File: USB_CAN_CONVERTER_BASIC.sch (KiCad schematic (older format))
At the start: 22 parts, among them P1 CONN_01X05, P2 CONN_01X02, P3 USB_A, P4 CONN_01X04, U1 STM32F042C6Ux, U2 PSD2CAN, U3 SN65HVD232D, U4 MCP1700T-3302E/TT, U5 USBLC6-2

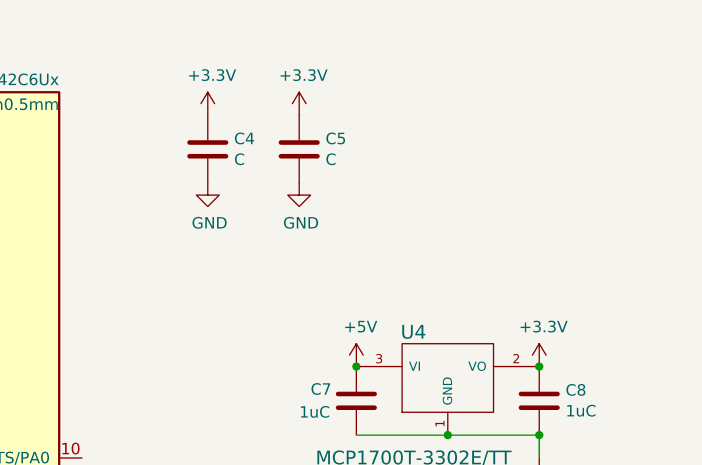
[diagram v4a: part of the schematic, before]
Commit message: Outline size reduction
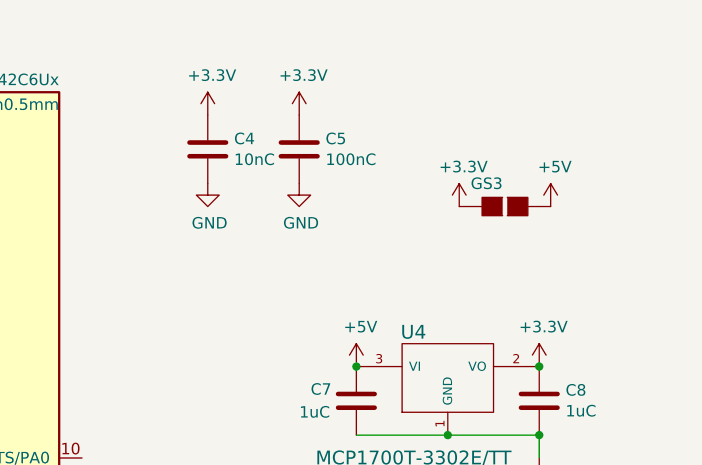
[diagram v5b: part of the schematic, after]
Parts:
- added GS3: GS2, Connect:GS2, symbol GS2
- C4: value C -> 10nC
- C5: value C -> 100nC
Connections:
- net +3V3: now also GS3.2 (G2)
- net +5V: now also GS3.1 (G1)
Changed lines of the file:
@@
 P 9100 1700
 F 0 "C4" H 9215 1746 50  0000 L CNN
-F 1 "C" H 9215 1655 50  0000 L CNN
+F 1 "10nC" H 9215 1655 50  0000 L CNN
 F 2 "Resistors_SMD:R_0805" H 9138 1550 50  0001 C CNN
 F 3 "" H 9100 1700 50  0000 C CNN
@@
 P 9500 1700
 F 0 "C5" H 9615 1746 50  0000 L CNN
-F 1 "C" H 9615 1655 50  0000 L CNN
+F 1 "100nC" H 9615 1655 50  0000 L CNN
 F 2 "Resistors_SMD:R_0805_HandSoldering" H 9538 1550 50  0001 C CNN
 F 3 "" H 9500 1700 50  0000 C CNN
@@
 	0    -1   -1   0
 $EndComp
+$Comp
+L GND #PWR15
+U 1 1 571ACD79
+P 9250 3350
+F 0 "#PWR15" H 9250 3100 50  0001 C CNN
+F 1 "GND" H 9350 3200 50  0000 C CNN
+F 2 "" H 9250 3350 50  0000 C CNN
+F 3 "" H 9250 3350 50  0000 C CNN
+	1    9250 3350
+	-1   0    0    1
+$EndComp
+$Comp
+L CONN_01X04 P4
+U 1 1 571E76C6
+P 9600 3500
+F 0 "P4" H 9677 3492 50  0000 L CNN
+F 1 "CONN_01X04" H 9678 3447 50  0001 L CNN
+F 2 "usb_ccb_custom:Pin_Header_Angled_1x04m" H 9677 3447 50  0001 L CNN
+F 3 "" H 9600 3500 50  0000 C CNN
+	1    9600 3500
+	1    0    0    -1
+$EndComp
+$Comp
+L +5V #PWR16
+U 1 1 571E7816
+P 9400 3350
+F 0 "#PWR16" H 9400 3200 50  0001 C CNN
+F 1 "+5V" H 9418 3523 50  0000 C CNN
+F 2 "" H 9400 3350 50  0000 C CNN
+F 3 "" H 9400 3350 50  0000 C CNN
+	1    9400 3350
+	1    0    0    -1
+$EndComp
+Text Label 8850 3550 0    60   ~ 0
+USART1_TX
+Text Label 8850 3650 0    60   ~ 0
+USART1_RX
+$Comp
+L CONN_01X05 P1
+U 1 1 57800591
+P 950 2050
+F 0 "P1" H 869 1711 50  0000 C CNN
+F 1 "CONN_01X05" H 869 1710 50  0001 C CNN
+F 2 "usb_ccb_custom:swd_smd_conn5" H 869 1711 50  0001 C CNN
+F 3 "" H 950 2050 50  0000 C CNN
+	1    950  2050
+	-1   0    0    1
+$EndComp
+$Comp
+L +3.3V #PWR1
+U 1 1 57800AA2
+P 1150 2250
+F 0 "#PWR1" H 1150 2100 50  0001 C CNN
+F 1 "+3.3V" H 1168 2423 50  0000 C CNN
+F 2 "" H 1150 2250 50  0000 C CNN
+F 3 "" H 1150 2250 50  0000 C CNN
+	1    1150 2250
+	0    1    1    0
+$EndComp
+$Comp
+L GS2 GS1
+U 1 1 5781392F
+P 1750 5850
+F 0 "GS1" H 1818 5850 50  0000 L CNN
+F 1 "GS2" H 1818 5850 50  0001 L CNN
+F 2 "Connect:GS2" H 1818 5805 50  0001 L CNN
+F 3 "" H 1750 5850 50  0000 C CNN
+	1    1750 5850
+	1    0    0    -1
+$EndComp
+$Comp
+L GS2 GS2
+U 1 1 57813F91
+P 2500 5850
+F 0 "GS2" H 2568 5850 50  0000 L CNN
+F 1 "GS2" H 2568 5850 50  0001 L CNN
+F 2 "Connect:GS2" H 2568 5805 50  0001 L CNN
+F 3 "" H 2500 5850 50  0000 C CNN
+	1    2500 5850
+	1    0    0    -1
+$EndComp
+$Comp
+L GS2 GS3
+U 1 1 57838B89
+P 10400 1950
+F 0 "GS3" V 10300 1800 50  0000 L CNN
+F 1 "GS2" H 10468 1950 50  0001 L CNN
+F 2 "Connect:GS2" H 10468 1905 50  0001 L CNN
+F 3 "" H 10400 1950 50  0000 C CNN
+	1    10400 1950
+	0    1    1    0
+$EndComp
+$Comp
+L +3.3V #PWR?
+U 1 1 578399EB
+P 10200 1950
+F 0 "#PWR?" H 10200 1800 50  0001 C CNN
+F 1 "+3.3V" H 10218 2123 50  0000 C CNN
+F 2 "" H 10200 1950 50  0000 C CNN
+F 3 "" H 10200 1950 50  0000 C CNN
+	1    10200 1950
+	1    0    0    -1
+$EndComp
 Wire Wire Line
 	5250 4950 5550 4950
@@
 Wire Wire Line
 	10500 4550 10600 4550
-$Comp
-L GND #PWR15
-U 1 1 571ACD79
-P 9250 3350
-F 0 "#PWR15" H 9250 3100 50  0001 C CNN
-F 1 "GND" H 9350 3200 50  0000 C CNN
-F 2 "" H 9250 3350 50  0000 C CNN
-F 3 "" H 9250 3350 50  0000 C CNN
-	1    9250 3350
-	-1   0    0    1
-$EndComp
-$Comp
-L CONN_01X04 P4
-U 1 1 571E76C6
-P 9600 3500
-F 0 "P4" H 9677 3492 50  0000 L CNN
-F 1 "CONN_01X04" H 9678 3447 50  0001 L CNN
-F 2 "usb_ccb_custom:Pin_Header_Angled_1x04m" H 9677 3447 50  0001 L CNN
-F 3 "" H 9600 3500 50  0000 C CNN
-	1    9600 3500
-	1    0    0    -1
-$EndComp
-$Comp
-L +5V #PWR16
-U 1 1 571E7816
-P 9400 3350
-F 0 "#PWR16" H 9400 3200 50  0001 C CNN
-F 1 "+5V" H 9418 3523 50  0000 C CNN
-F 2 "" H 9400 3350 50  0000 C CNN
-F 3 "" H 9400 3350 50  0000 C CNN
-	1    9400 3350
-	1    0    0    -1
-$EndComp
-Text Label 8850 3550 0    60   ~ 0
-USART1_TX
 Wire Wire Line
 	9250 3450 9400 3450
 Wire Wire Line
 	9250 3450 9250 3350
-Text Label 8850 3650 0    60   ~ 0
-USART1_RX
 Connection ~ 1950 1850
 Wire Wire Line
@@
 Wire Wire Line
 	8850 4050 8850 3650
-$Comp
-L CONN_01X05 P1
-U 1 1 57800591
-P 950 2050
-F 0 "P1" H 869 1711 50  0000 C CNN
-F 1 "CONN_01X05" H 869 1710 50  0001 C CNN
-F 2 "usb_ccb_custom:swd_smd_conn5" H 869 1711 50  0001 C CNN
-F 3 "" H 950 2050 50  0000 C CNN
-	1    950  2050
-	-1   0    0    1
-$EndComp
-$Comp
-L +3.3V #PWR1
-U 1 1 57800AA2
-P 1150 2250
-F 0 "#PWR1" H 1150 2100 50  0001 C CNN
-F 1 "+3.3V" H 1168 2423 50  0000 C CNN
-F 2 "" H 1150 2250 50  0000 C CNN
-F 3 "" H 1150 2250 50  0000 C CNN
-	1    1150 2250
-	0    1    1    0
-$EndComp
 Wire Wire Line
 	1150 2050 1450 2050
@@
 	1450 1850 1150 1850
 Connection ~ 2700 5550
-$Comp
-L GS2 GS1
-U 1 1 5781392F
-P 1750 5850
-F 0 "GS1" H 1818 5850 50  0000 L CNN
-F 1 "GS2" H 1818 5850 50  0001 L CNN
-F 2 "Connect:GS2" H 1818 5805 50  0001 L CNN
-F 3 "" H 1750 5850 50  0000 C CNN
-	1    1750 5850
-	1    0    0    -1
-$EndComp
 Wire Wire Line
 	2150 5550 2150 5650
@@
 Wire Wire Line
 	1750 6050 1750 6200
-$Comp
-L GS2 GS2
-U 1 1 57813F91
-P 2500 5850
-F 0 "GS2" H 2568 5850 50  0000 L CNN
-F 1 "GS2" H 2568 5850 50  0001 L CNN
-F 2 "Connect:GS2" H 2568 5805 50  0001 L CNN
-F 3 "" H 2500 5850 50  0000 C CNN
-	1    2500 5850
-	1    0    0    -1
-$EndComp
 Wire Wire Line
 	2500 6050 2500 6100
+$Comp
+L +5V #PWR?
+U 1 1 5783A2C6
+P 10600 1950
+F 0 "#PWR?" H 10600 1800 50  0001 C CNN
+F 1 "+5V" H 10618 2123 50  0000 C CNN
+F 2 "" H 10600 1950 50  0000 C CNN
+F 3 "" H 10600 1950 50  0000 C CNN
+	1    10600 1950
+	1    0    0    -1
+$EndComp
 $EndSCHEMATC

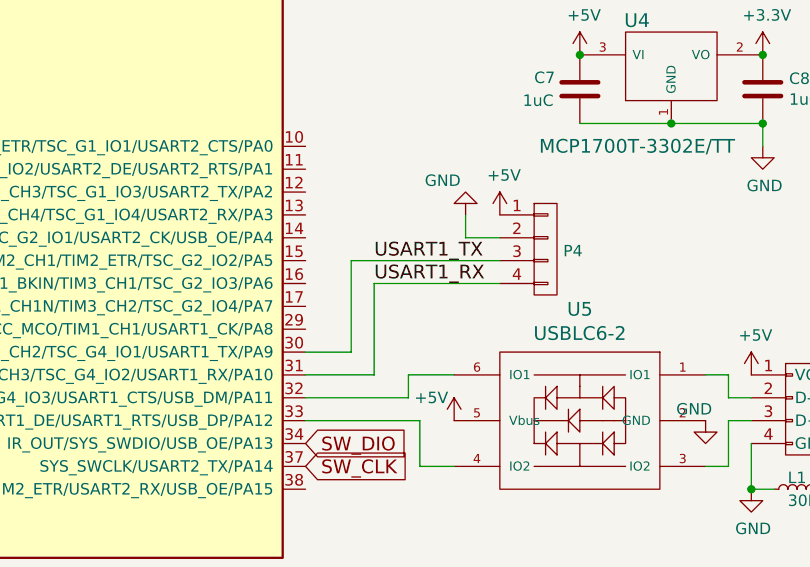
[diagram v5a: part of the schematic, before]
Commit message: USART change
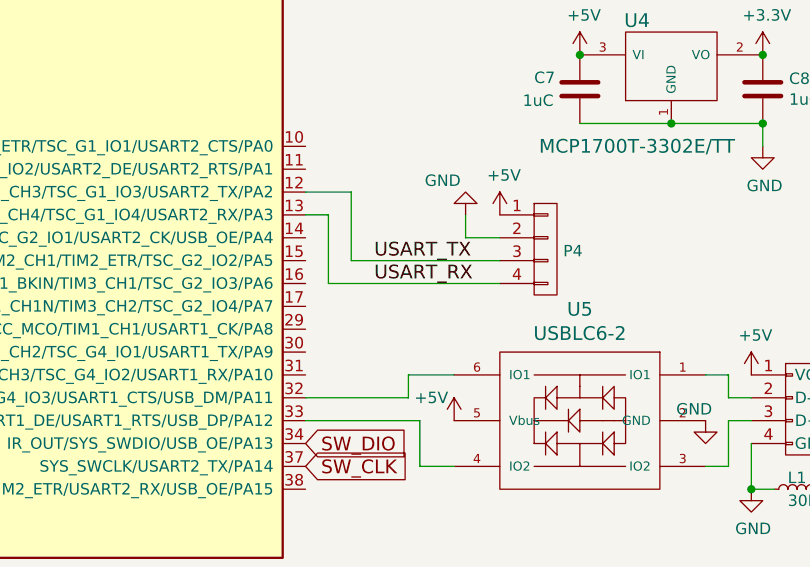
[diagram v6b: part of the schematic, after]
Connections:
- net USART_TX: now reaches U1.12 (ADC_IN2/SYS_WKUP4/TIM2_CH3/TSC_G1_IO3/USART2_TX/PA2)
- net USART_TX: now also P4.3 (P3)
- net USART_RX: now reaches U1.13 (ADC_IN3/TIM2_CH4/TSC_G1_IO4/USART2_RX/PA3)
- net USART_RX: now also P4.4 (P4)
- net USART1_RX: no longer names the net of U1.31 (I2C1_SDA/TIM17_BKIN/TIM1_CH3/TSC_G4_IO2/USART1_RX/PA10)
- net USART1_RX: no longer P4.4 (P4)
- net USART1_TX: no longer names the net of U1.30 (I2C1_SCL/TIM1_CH2/TSC_G4_IO1/USART1_TX/PA9)
- net USART1_TX: no longer P4.3 (P3)
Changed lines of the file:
@@
 $EndComp
 $Comp
-L GND #PWR11
+L GND #PWR01
 U 1 1 570561B2
 P 5250 4950
-F 0 "#PWR11" H 5250 4700 50  0001 C CNN
+F 0 "#PWR01" H 5250 4700 50  0001 C CNN
 F 1 "GND" H 5258 4777 50  0000 C CNN
 F 2 "" H 5250 4950 50  0000 C CNN
@@
 SWCLK\nGND\nSWDIO\nNRST\nVTRG
 $Comp
-L GND #PWR3
+L GND #PWR02
 U 1 1 57056C83
 P 1600 1950
-F 0 "#PWR3" H 1600 1700 50  0001 C CNN
+F 0 "#PWR02" H 1600 1700 50  0001 C CNN
 F 1 "GND" V 1608 1822 50  0000 R CNN
 F 2 "" H 1600 1950 50  0000 C CNN
@@
 $EndComp
 $Comp
-L GND #PWR22
+L GND #PWR03
 U 1 1 5706C070
 P 10500 4550
-F 0 "#PWR22" H 10500 4300 50  0001 C CNN
+F 0 "#PWR03" H 10500 4300 50  0001 C CNN
 F 1 "GND" H 10508 4377 50  0000 C CNN
 F 2 "" H 10500 4550 50  0000 C CNN
@@
 $EndComp
 $Comp
-L +5V #PWR21
+L +5V #PWR04
 U 1 1 5706C74A
 P 10500 4050
-F 0 "#PWR21" H 10500 3900 50  0001 C CNN
+F 0 "#PWR04" H 10500 3900 50  0001 C CNN
 F 1 "+5V" H 10518 4223 50  0000 C CNN
 F 2 "" H 10500 4050 50  0000 C CNN
@@
 $EndComp
 $Comp
-L +5V #PWR19
+L +5V #PWR05
 U 1 1 5706E498
 P 9750 2650
-F 0 "#PWR19" H 9750 2500 50  0001 C CNN
+F 0 "#PWR05" H 9750 2500 50  0001 C CNN
 F 1 "+5V" H 9768 2823 50  0000 C CNN
 F 2 "" H 9750 2650 50  0000 C CNN
@@
 $EndComp
 $Comp
-L +3.3V #PWR4
+L +3.3V #PWR06
 U 1 1 5706E500
 P 1950 1550
-F 0 "#PWR4" H 1950 1400 50  0001 C CNN
+F 0 "#PWR06" H 1950 1400 50  0001 C CNN
 F 1 "+3.3V" H 1968 1723 50  0000 C CNN
 F 2 "" H 1950 1550 50  0000 C CNN
@@
 $EndComp
 $Comp
-L +3.3V #PWR10
+L +3.3V #PWR07
 U 1 1 5706E57B
 P 5250 1350
-F 0 "#PWR10" H 5250 1200 50  0001 C CNN
+F 0 "#PWR07" H 5250 1200 50  0001 C CNN
 F 1 "+3.3V" H 5268 1523 50  0000 C CNN
 F 2 "" H 5250 1350 50  0000 C CNN
@@
 $EndComp
 $Comp
-L +3.3V #PWR23
+L +3.3V #PWR08
 U 1 1 5706E6F4
 P 10550 2650
-F 0 "#PWR23" H 10550 2500 50  0001 C CNN
+F 0 "#PWR08" H 10550 2500 50  0001 C CNN
 F 1 "+3.3V" H 10568 2823 50  0000 C CNN
 F 2 "" H 10550 2650 50  0000 C CNN
@@
 $EndComp
 $Comp
-L GND #PWR13
+L GND #PWR09
 U 1 1 5706EDB2
 P 9100 1850
-F 0 "#PWR13" H 9100 1600 50  0001 C CNN
+F 0 "#PWR09" H 9100 1600 50  0001 C CNN
 F 1 "GND" H 9108 1677 50  0000 C CNN
 F 2 "" H 9100 1850 50  0000 C CNN
@@
 $EndComp
 $Comp
-L GND #PWR18
+L GND #PWR010
 U 1 1 5706EDDA
 P 9500 1850
-F 0 "#PWR18" H 9500 1600 50  0001 C CNN
+F 0 "#PWR010" H 9500 1600 50  0001 C CNN
 F 1 "GND" H 9508 1677 50  0000 C CNN
 F 2 "" H 9500 1850 50  0000 C CNN
@@
 $EndComp
 $Comp
-L +3.3V #PWR17
+L +3.3V #PWR011
 U 1 1 5706EE52
 P 9500 1550
-F 0 "#PWR17" H 9500 1400 50  0001 C CNN
+F 0 "#PWR011" H 9500 1400 50  0001 C CNN
 F 1 "+3.3V" H 9518 1723 50  0000 C CNN
 F 2 "" H 9500 1550 50  0000 C CNN
@@
 $EndComp
 $Comp
-L +3.3V #PWR12
+L +3.3V #PWR012
 U 1 1 5706EEDE
 P 9100 1550
-F 0 "#PWR12" H 9100 1400 50  0001 C CNN
+F 0 "#PWR012" H 9100 1400 50  0001 C CNN
 F 1 "+3.3V" H 9118 1723 50  0000 C CNN
 F 2 "" H 9100 1550 50  0000 C CNN
@@
 $EndComp
 $Comp
-L GND #PWR24
+L GND #PWR013
 U 1 1 5706F734
 P 10550 3050
-F 0 "#PWR24" H 10550 2800 50  0001 C CNN
+F 0 "#PWR013" H 10550 2800 50  0001 C CNN
 F 1 "GND" H 10558 2877 50  0000 C CNN
 F 2 "" H 10550 3050 50  0000 C CNN
@@
 $EndComp
 $Comp
-L +3.3V #PWR8
+L +3.3V #PWR014
 U 1 1 5708A6C5
 P 4750 6100
-F 0 "#PWR8" H 4750 5950 50  0001 C CNN
+F 0 "#PWR014" H 4750 5950 50  0001 C CNN
 F 1 "+3.3V" H 4768 6273 50  0000 C CNN
 F 2 "" H 4750 6100 50  0000 C CNN
@@
 $EndComp
 $Comp
-L GND #PWR9
+L GND #PWR015
 U 1 1 5708A9FB
 P 4750 6400
-F 0 "#PWR9" H 4750 6150 50  0001 C CNN
+F 0 "#PWR015" H 4750 6150 50  0001 C CNN
 F 1 "GND" V 4758 6272 50  0000 R CNN
 F 2 "" H 4750 6400 50  0000 C CNN
@@
 $EndComp
 $Comp
-L GND #PWR7
+L GND #PWR016
 U 1 1 5708B621
 P 4450 6400
-F 0 "#PWR7" H 4450 6150 50  0001 C CNN
+F 0 "#PWR016" H 4450 6150 50  0001 C CNN
 F 1 "GND" V 4458 6272 50  0000 R CNN
 F 2 "" H 4450 6400 50  0000 C CNN
@@
 $EndComp
 $Comp
-L GND #PWR6
+L GND #PWR017
 U 1 1 5708BDA5
 P 4200 6400
-F 0 "#PWR6" H 4200 6150 50  0001 C CNN
+F 0 "#PWR017" H 4200 6150 50  0001 C CNN
 F 1 "GND" V 4208 6272 50  0000 R CNN
 F 2 "" H 4200 6400 50  0000 C CNN
@@
 $EndComp
 $Comp
-L GND #PWR2
+L GND #PWR018
 U 1 1 5708D67B
 P 1450 7100
-F 0 "#PWR2" H 1450 6850 50  0001 C CNN
+F 0 "#PWR018" H 1450 6850 50  0001 C CNN
 F 1 "GND" V 1458 6972 50  0000 R CNN
 F 2 "" H 1450 7100 50  0000 C CNN
@@
 $EndComp
 $Comp
-L GND #PWR5
+L GND #PWR019
 U 1 1 5708E325
 P 3000 5550
-F 0 "#PWR5" H 3000 5300 50  0001 C CNN
+F 0 "#PWR019" H 3000 5300 50  0001 C CNN
 F 1 "GND" V 3008 5422 50  0000 R CNN
 F 2 "" H 3000 5550 50  0000 C CNN
@@
 $EndComp
 $Comp
-L +5V #PWR14
+L +5V #PWR020
 U 1 1 5716787A
 P 9200 4250
-F 0 "#PWR14" H 9200 4100 50  0001 C CNN
+F 0 "#PWR020" H 9200 4100 50  0001 C CNN
 F 1 "+5V" H 9100 4350 50  0000 C CNN
 F 2 "" H 9200 4250 50  0000 C CNN
@@
 $EndComp
 $Comp
-L GND #PWR20
+L GND #PWR021
 U 1 1 57167911
 P 10300 4250
-F 0 "#PWR20" H 10300 4000 50  0001 C CNN
+F 0 "#PWR021" H 10300 4000 50  0001 C CNN
 F 1 "GND" H 10250 4300 50  0000 C CNN
 F 2 "" H 10300 4250 50  0000 C CNN
@@
 $EndComp
 $Comp
-L GND #PWR15
+L GND #PWR022
 U 1 1 571ACD79
 P 9250 3350
-F 0 "#PWR15" H 9250 3100 50  0001 C CNN
+F 0 "#PWR022" H 9250 3100 50  0001 C CNN
 F 1 "GND" H 9350 3200 50  0000 C CNN
 F 2 "" H 9250 3350 50  0000 C CNN
@@
 $EndComp
 $Comp
-L +5V #PWR16
+L +5V #PWR023
 U 1 1 571E7816
 P 9400 3350
-F 0 "#PWR16" H 9400 3200 50  0001 C CNN
+F 0 "#PWR023" H 9400 3200 50  0001 C CNN
 F 1 "+5V" H 9418 3523 50  0000 C CNN
 F 2 "" H 9400 3350 50  0000 C CNN
@@
 $EndComp
 Text Label 8850 3550 0    60   ~ 0
-USART1_TX
+USART_TX
 Text Label 8850 3650 0    60   ~ 0
-USART1_RX
+USART_RX
 $Comp
 L CONN_01X05 P1
@@
 $EndComp
 $Comp
-L +3.3V #PWR1
+L +3.3V #PWR024
 U 1 1 57800AA2
 P 1150 2250
-F 0 "#PWR1" H 1150 2100 50  0001 C CNN
+F 0 "#PWR024" H 1150 2100 50  0001 C CNN
 F 1 "+3.3V" H 1168 2423 50  0000 C CNN
 F 2 "" H 1150 2250 50  0000 C CNN
@@
 $EndComp
 $Comp
-L +3.3V #PWR?
+L +3.3V #PWR025
 U 1 1 578399EB
 P 10200 1950
-F 0 "#PWR?" H 10200 1800 50  0001 C CNN
+F 0 "#PWR025" H 10200 1800 50  0001 C CNN
 F 1 "+3.3V" H 10218 2123 50  0000 C CNN
 F 2 "" H 10200 1950 50  0000 C CNN
@@
 Connection ~ 1950 1850
 Wire Wire Line
-	8850 3650 9400 3650
-Wire Wire Line
-	8550 3950 8750 3950
-Wire Wire Line
-	8750 3950 8750 3550
+	8650 3650 9400 3650
 Wire Wire Line
 	8750 3550 9400 3550
-Wire Wire Line
-	8550 4050 8850 4050
-Wire Wire Line
-	8850 4050 8850 3650
 Wire Wire Line
 	1150 2050 1450 2050
@@
 	2500 6050 2500 6100
 $Comp
-L +5V #PWR?
+L +5V #PWR026
 U 1 1 5783A2C6
 P 10600 1950
-F 0 "#PWR?" H 10600 1800 50  0001 C CNN
+F 0 "#PWR026" H 10600 1800 50  0001 C CNN
 F 1 "+5V" H 10618 2123 50  0000 C CNN
 F 2 "" H 10600 1950 50  0000 C CNN
@@
 	1    0    0    -1
 $EndComp
+Wire Wire Line
+	8750 3550 8750 3250
+Wire Wire Line
+	8750 3250 8550 3250
+Wire Wire Line
+	8650 3650 8650 3350
+Wire Wire Line
+	8650 3350 8550 3350
 $EndSCHEMATC

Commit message: Board rooting done.
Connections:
- net at GS2.2 (G2), P2.1 (P1), U3.6 (CANL): now also U2.2 (C2); no longer U2.1 (C1)
- net at GS1.2 (G2), P2.2 (P2), U3.7 (CANH): now also U2.1 (C1); no longer U2.2 (C2)
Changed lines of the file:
@@
 F 3 "" H 1450 6950 60  0000 C CNN
 	1    1450 6750
-	1    0    0    -1
+	-1   0    0    -1
 $EndComp
 $Comp

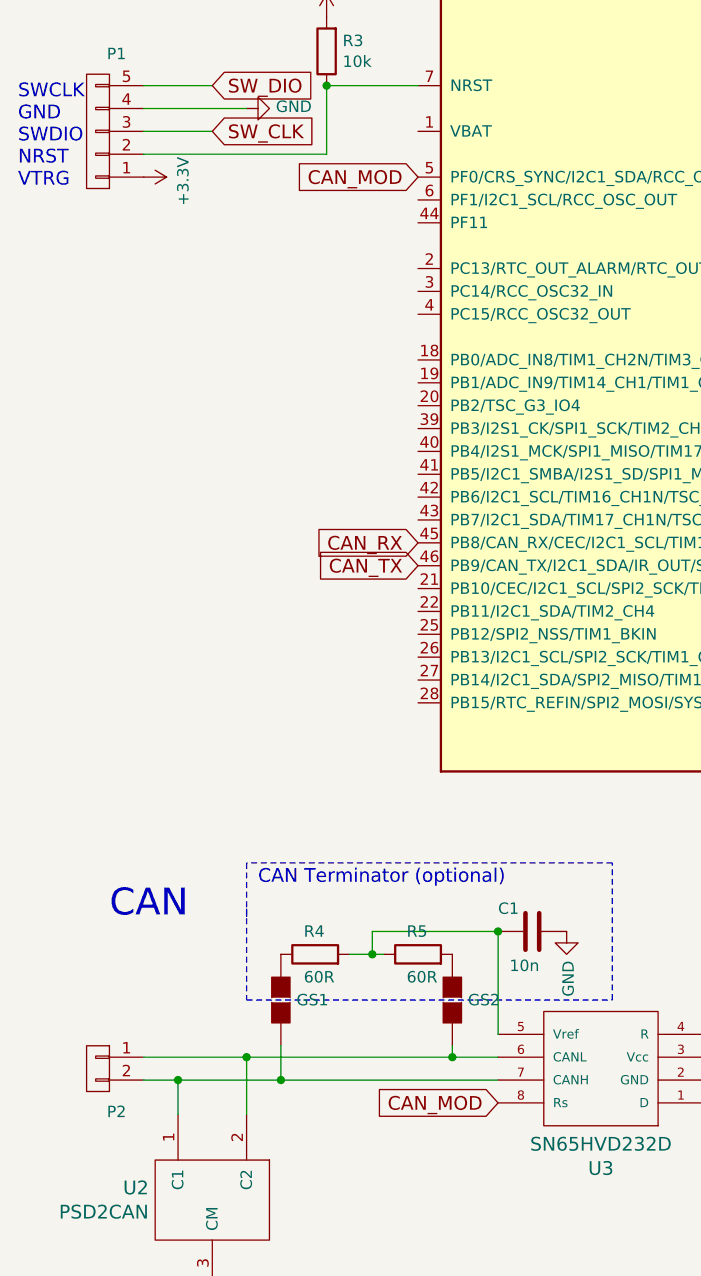
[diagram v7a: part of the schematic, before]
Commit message: Rooting and CANmod replace.
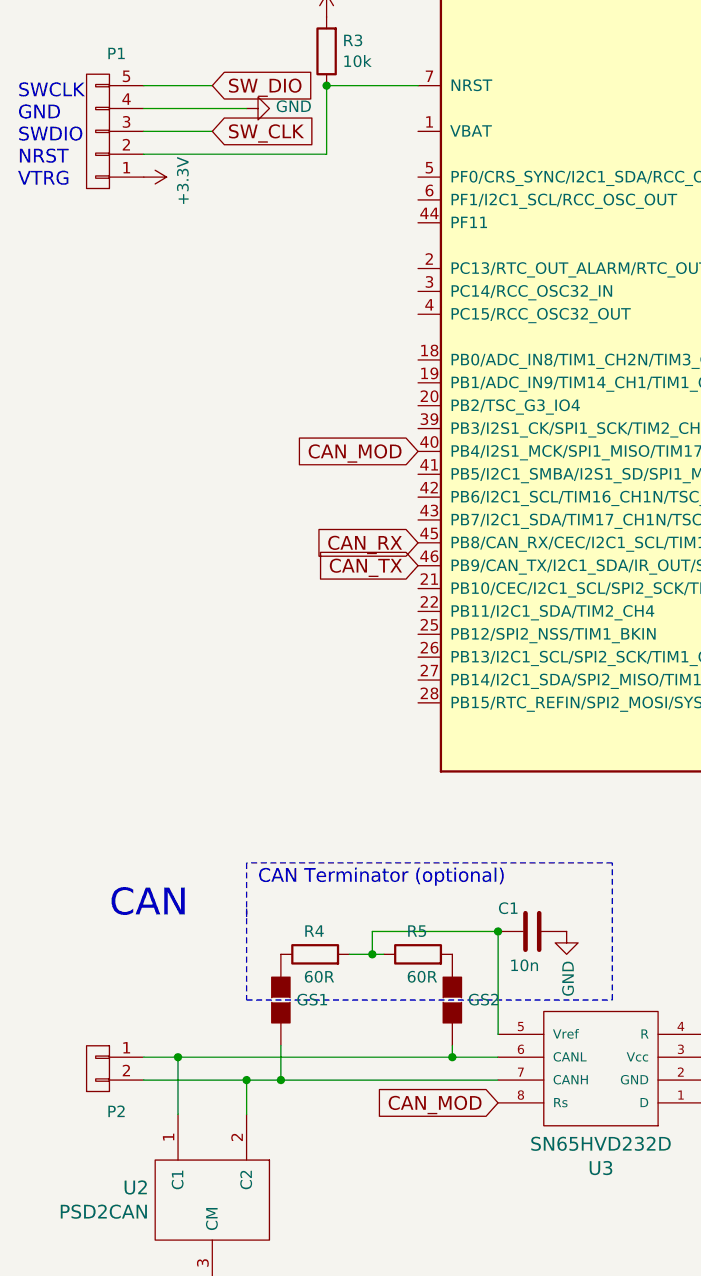
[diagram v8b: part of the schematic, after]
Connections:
- net CAN_MOD: now also U1.40 (PB4/I2S1_MCK/SPI1_MISO/TIM17_BKIN/TIM3_CH1/TSC_G5_IO2); no longer U1.5 (PF0/CRS_SYNC/I2C1_SDA/RCC_OSC_IN)
- net at GS2.2 (G2), P2.1 (P1), U3.6 (CANL): now also U2.1 (C1); no longer U2.2 (C2)
- net at GS1.2 (G2), P2.2 (P2), U3.7 (CANH): now also U2.2 (C2); no longer U2.1 (C1)
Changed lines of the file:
@@
 Text GLabel 2350 3850 0    60   Input ~ 0
 CAN_RX
-Text GLabel 2350 2250 0    60   Input ~ 0
+Text GLabel 2350 3450 0    60   Input ~ 0
 CAN_MOD
 Text GLabel 2700 6300 0    60   Input ~ 0
@@
 	3600 6100 4750 6100
 Wire Wire Line
-	1300 6350 1300 6200
-Wire Wire Line
 	1150 6200 2700 6200
 Wire Wire Line
-	1600 6100 1600 6350
-Wire Wire Line
 	1150 6100 2700 6100
-Connection ~ 1600 6100
-Connection ~ 1300 6200
 Connection ~ 2500 6100
 Connection ~ 1750 6200
@@
 Wire Wire Line
 	8650 3350 8550 3350
+Wire Wire Line
+	1300 6350 1300 6100
+Connection ~ 1300 6100
+Wire Wire Line
+	1600 6350 1600 6200
+Connection ~ 1600 6200
 $EndSCHEMATC
